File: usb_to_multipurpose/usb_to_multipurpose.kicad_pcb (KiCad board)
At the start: 2 copper layers, 27 x 29.1 mm, 35 parts, among them U1 FT232H, U2 AP2112K-3.3TRG1, U5 93LC56BT-I/OT, Y1 12MHz

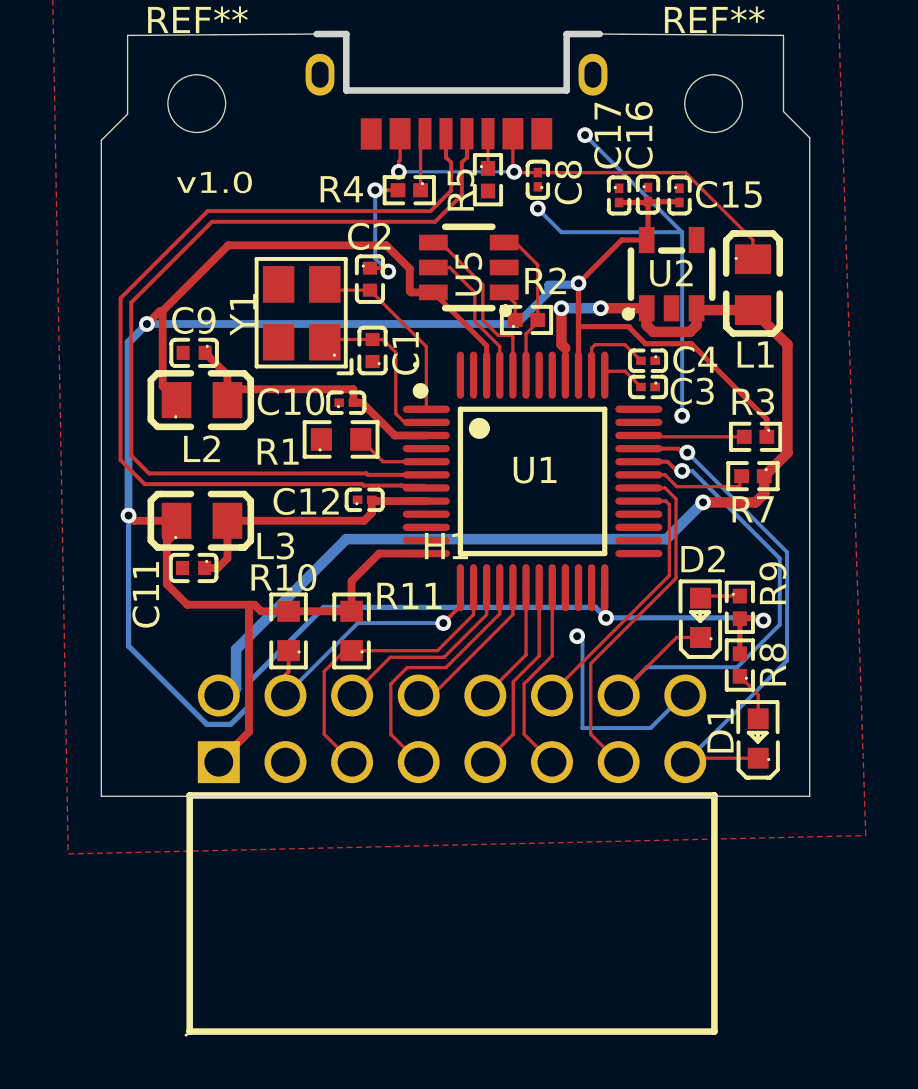
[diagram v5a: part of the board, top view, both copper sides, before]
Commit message: Change connector for smaller JST SH 2x6 pin.
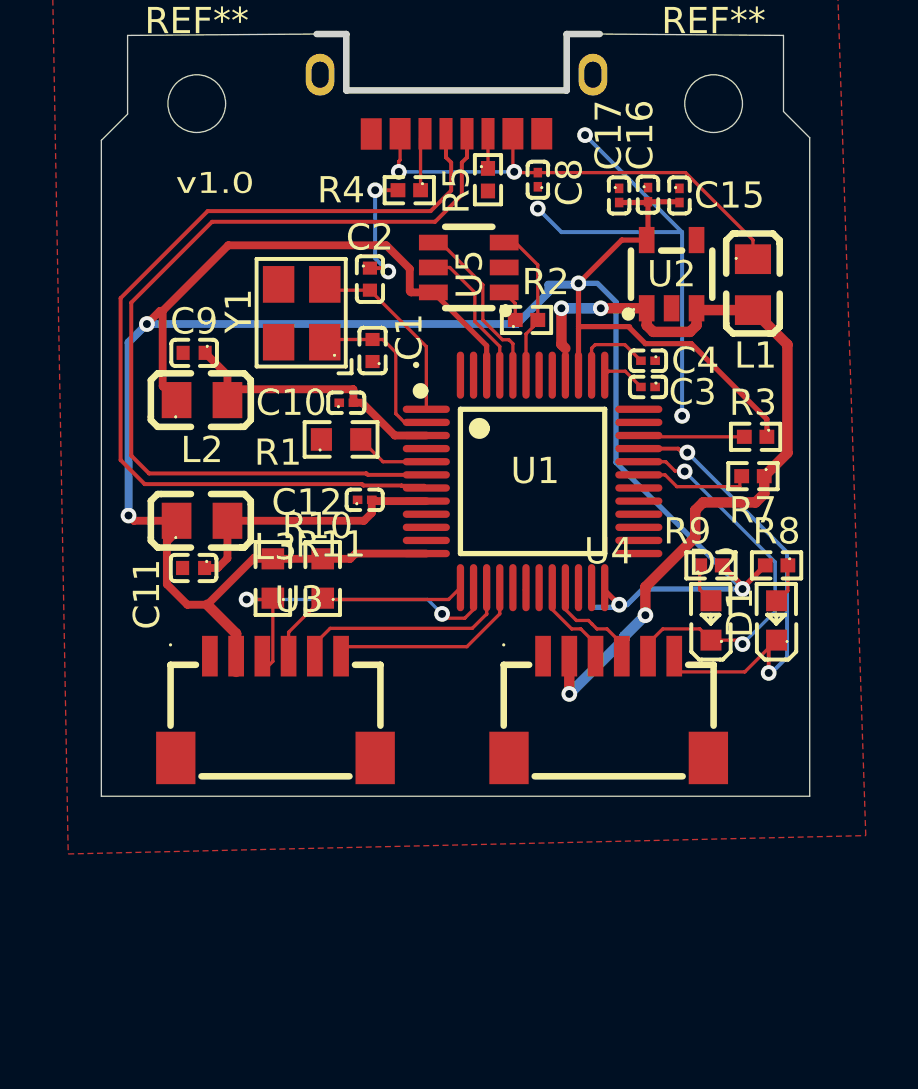
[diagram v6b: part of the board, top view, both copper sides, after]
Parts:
- removed H1: HDR2.54-2*8PW, easyeda2kicad:HDR-TH_16P-P2.54-H-F-R2-C8-S2.54-W10.0
- added U3: SM06B-SRSS-TB, easyeda2kicad:CONN-SMD_SM06B-SRSS-TB-LF-SN, F.Cu at (48.3, 60.3)
- added U4: SM06B-SRSS-TB, easyeda2kicad:CONN-SMD_SM06B-SRSS-TB-LF-SN, F.Cu at (61.0, 60.3)
- moved D1 4.55 mm to (67.4, 57.0)
- moved R8 4.05 mm to (67.4, 54.9), turned to 180 degrees
- moved R11 3.61 mm to (48.2, 55.4)
- moved R10 2.39 mm to (50.1, 55.4)
- moved R9 1.94 mm to (64.9, 54.9), turned to 0 degrees
- moved D2 0.41 mm to (64.9, 57.0)
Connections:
- U1 pad 17: Net-(U1-ADBUS4) -> unconnected-(U1-ADBUS4-Pad17)
- U1 pad 18: Net-(U1-ADBUS5) -> unconnected-(U1-ADBUS5-Pad18)
- U1 pad 19: Net-(U1-ADBUS6) -> unconnected-(U1-ADBUS6-Pad19)
- U1 pad 21: unconnected-(U1-ACBUS0-Pad21) -> Net-(U1-ACBUS0)
- U1 pad 29: Net-(U1-ACBUS5) -> unconnected-(U1-ACBUS5-Pad29)
- U1 pad 30: Net-(U1-ACBUS6) -> unconnected-(U1-ACBUS6-Pad30)
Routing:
- net VCC: track 125.7 -> 108.9 mm
- net Net-(U1-ACBUS6): track 13.4 -> 0.00 mm
- net +5V: track 43.6 -> 31.1 mm, vias 3 -> 4
- net Net-(U1-ACBUS5): track 10.4 -> 0.00 mm
- net GND: track 31.1 -> 23.0 mm, vias 6 -> 5
- net Net-(U1-ADBUS6): track 7.47 -> 0.00 mm
- net Net-(U1-ADBUS4): track 5.89 -> 0.00 mm
- net Net-(D2-K): track 20.7 -> 15.0 mm, vias 1 -> 2
- net Net-(U1-ADBUS5): track 4.86 -> 0.00 mm
- net Net-(U1-ACBUS0): track 0.00 -> 4.60 mm
- net Net-(U1-ADBUS7): track 7.54 -> 4.36 mm
- net /SDA/MOSI: track 11.5 -> 14.5 mm, vias 0 -> 2
- net /SDA/MISO: track 7.43 -> 9.38 mm
- net Net-(D1-K): track 19.7 -> 18.1 mm, vias 1 -> 2
- net /CS: track 9.68 -> 8.47 mm
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
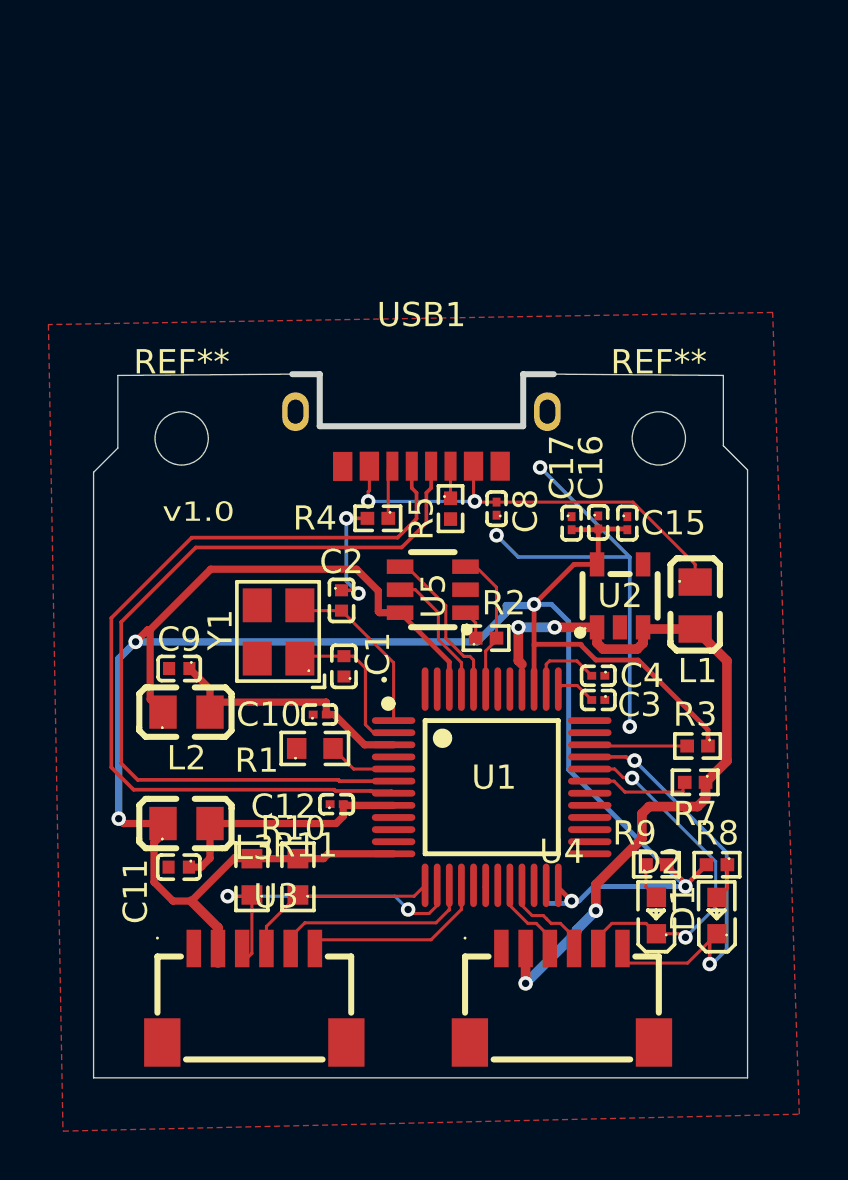
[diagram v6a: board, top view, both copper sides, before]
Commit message: Add comments and improve readability of the schematic
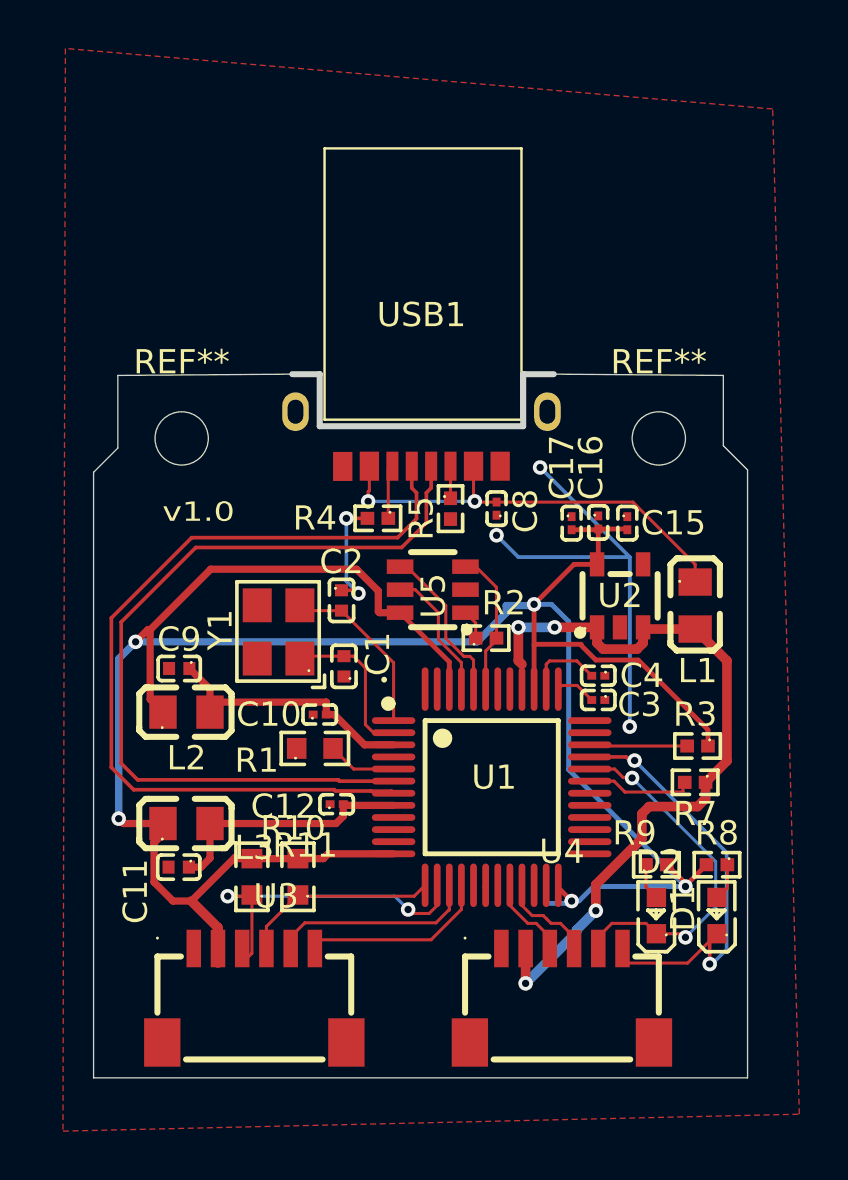
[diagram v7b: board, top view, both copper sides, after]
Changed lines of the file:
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@@
 		(sheetname "/")
 		(sheetfile "usb_to_multipurpose.kicad_sch")
-		(units
-			(unit
-				(name "A")
-				(pins "A12B1" "A9B4" "B5" "A7" "A6" "A5" "A4B9" "A1B12" "1" "2")
-			)
-		)
 		(attr smd)
 		(duplicate_pad_numbers_are_jumpers no)
 		(fp_line
+			(start -4 -12)
+			(end 4.13 -12)
+			(stroke
+				(width 0.1)
+				(type default)
+			)
+			(layer "F.SilkS")
+		)
+		(fp_line
+			(start -4 -0.8)
+			(end -4 -12)
+			(stroke
+				(width 0.1)
+				(type default)
+			)
+			(layer "F.SilkS")
+		)
+		(fp_line
+			(start 4.13 -12)
+			(end 4.13 -0.8)
+			(stroke
+				(width 0.1)
+				(type default)
+			)
+			(layer "F.SilkS")
+		)
+		(fp_line
+			(start 4.13 -0.8)
+			(end -4 -0.8)
+			(stroke
+				(width 0.1)
+				(type default)
+			)
+			(layer "F.SilkS")
+		)
+		(fp_line
 			(start -4.2 -2.68)
 			(end -5.33 -2.68)
@@
 		(model "${EASYEDA2KICAD}/easyeda2kicad.3dshapes/USB-C-SMD_HYCW675-USBC12-105B.wrl"
 			(offset
-				(xyz 0 0 -0.25)
+				(xyz 0 0 0)
 			)
 			(scale
@@
 		)
 		(min_thickness 0.1)
-		(fill yes
+		(fill
 			(thermal_gap 0.5)
 			(thermal_bridge_width 0.5)
@@
 		(polygon
 			(pts
-				(xy 39.8 32.6) (xy 40.4 65.9) (xy 70.8 65.2) (xy 69.7 32.1)
+				(xy 40.5 21.2) (xy 40.4 65.9) (xy 70.8 65.2) (xy 69.7 23.7)
 			)
 		)
